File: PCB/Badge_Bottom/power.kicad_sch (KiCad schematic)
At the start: 10 parts, among them J2 BAT, SW3 MSK12C02-HB, U1 TP4054, U3 AMS1117-3.3

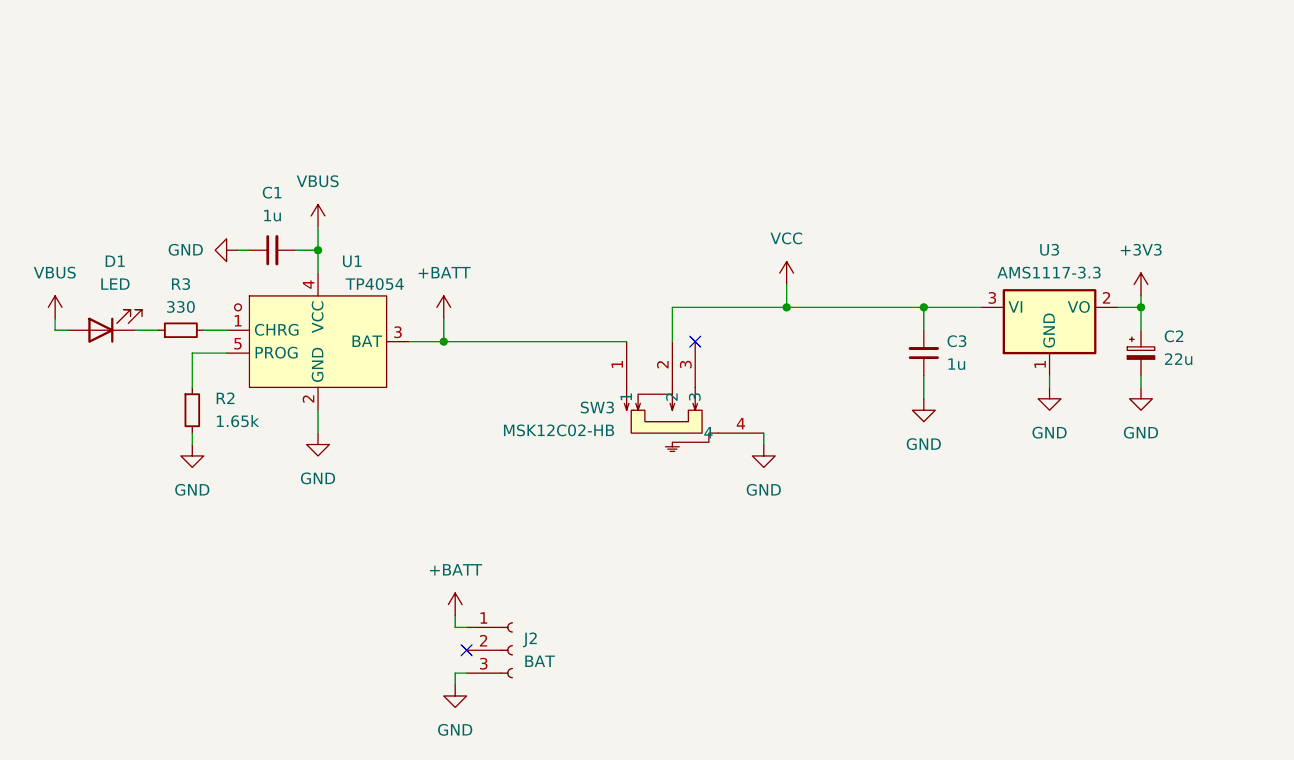
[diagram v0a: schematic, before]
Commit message: Added new page for IO, added new components, added JLC parts, fixed PCB standoffs to be pads and modified concept of PCB (dual usbc)
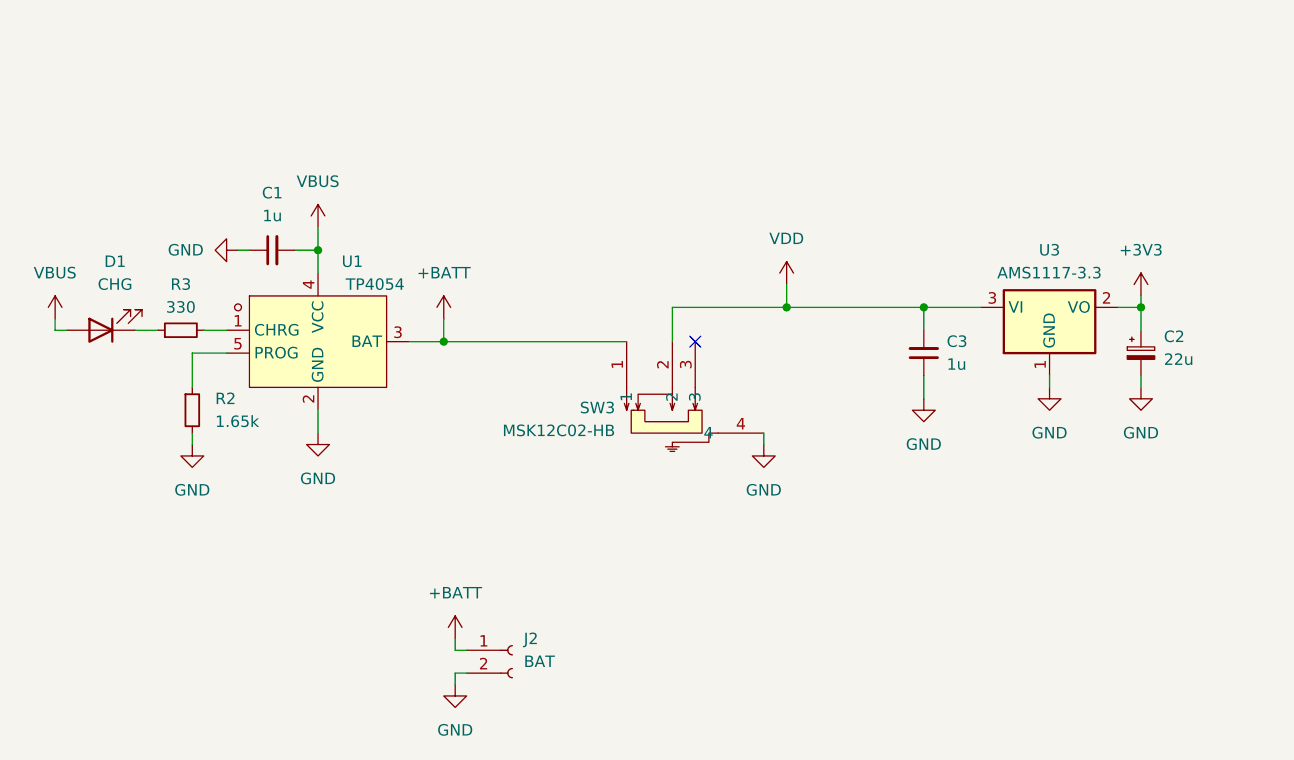
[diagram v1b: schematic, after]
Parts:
- C1, C2, C3: footprint (none) -> Capacitor_SMD:C_0603_1608Metric
- D1: value LED -> CHG; footprint (none) -> LED_SMD:LED_0603_1608Metric
- J2: footprint (none) -> Connector_JST:JST_PH_S2B-PH-SM4-TB_1x02-1MP_P2.00mm_Horizontal; symbol Connector:Conn_01x03_Socket -> Connector:Conn_01x02_Socket
- R2, R3: footprint (none) -> Resistor_SMD:R_0603_1608Metric
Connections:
- net GND: now also J2.2 (Pin_2); no longer J2.3 (Pin_3)
- net VCC renamed VDD
- no-connect marks 2 -> 1
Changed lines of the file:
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@@
   )
   (no_connect (at 148.59 100.33))
-  (no_connect (at 123.19 134.62))
-  (wire (pts (xy 123.19 132.08) (xy 121.92 132.08))
-    (stroke (width 0) (type default))
-  )
   (wire (pts (xy 146.05 96.52) (xy 158.75 96.52))
     (stroke (width 0) (type default))
@@
     (stroke (width 0) (type default))
   )
-  (wire (pts (xy 121.92 130.81) (xy 121.92 132.08))
-    (stroke (width 0) (type default))
-  )
   (wire (pts (xy 120.65 100.33) (xy 120.65 97.79))
     (stroke (width 0) (type default))
@@
     (stroke (width 0) (type default))
   )
+  (wire (pts (xy 123.19 134.62) (xy 121.92 134.62))
+    (stroke (width 0) (type default))
+  )
   (wire (pts (xy 198.12 96.52) (xy 198.12 99.06))
     (stroke (width 0) (type default))
@@
     (stroke (width 0) (type default))
   )
+  (wire (pts (xy 121.92 134.62) (xy 121.92 133.35))
+    (stroke (width 0) (type default))
+  )
   (wire (pts (xy 97.79 90.17) (xy 99.06 90.17))
     (stroke (width 0) (type default))
@@
     (stroke (width 0) (type default))
   )
-  (symbol (lib_id "power:+BATT") (at 121.92 130.81 0) (unit 1)
-    (in_bom yes) (on_board yes) (dnp no) (fields_autoplaced)
-    (property "Reference" "#PWR07" (at 121.92 134.62 0)
-      (effects (font (size 1.27 1.27)) hide)
-    )
-    (property "Value" "+BATT" (at 121.92 125.73 0)
-      (effects (font (size 1.27 1.27)))
-    )
-    (property "Footprint" "" (at 121.92 130.81 0)
-      (effects (font (size 1.27 1.27)) hide)
-    )
-    (property "Datasheet" "" (at 121.92 130.81 0)
+  (symbol (lib_id "power:+BATT") (at 121.92 133.35 0) (unit 1)
+    (in_bom yes) (on_board yes) (dnp no) (fields_autoplaced)
+    (property "Reference" "#PWR07" (at 121.92 137.16 0)
+      (effects (font (size 1.27 1.27)) hide)
+    )
+    (property "Value" "+BATT" (at 121.92 128.27 0)
+      (effects (font (size 1.27 1.27)))
+    )
+    (property "Footprint" "" (at 121.92 133.35 0)
+      (effects (font (size 1.27 1.27)) hide)
+    )
+    (property "Datasheet" "" (at 121.92 133.35 0)
       (effects (font (size 1.27 1.27)) hide)
     )
@@
       (effects (font (size 1.27 1.27)))
     )
-    (property "Footprint" "" (at 91.44 99.06 0)
+    (property "Footprint" "Resistor_SMD:R_0603_1608Metric" (at 91.44 99.06 0)
       (effects (font (size 1.27 1.27)) hide)
     )
@@
     )
   )
+  (symbol (lib_id "power:VDD") (at 158.75 93.98 0) (unit 1)
+    (in_bom yes) (on_board yes) (dnp no) (fields_autoplaced)
+    (property "Reference" "#PWR03" (at 158.75 97.79 0)
+      (effects (font (size 1.27 1.27)) hide)
+    )
+    (property "Value" "VDD" (at 158.75 88.9 0)
+      (effects (font (size 1.27 1.27)))
+    )
+    (property "Footprint" "" (at 158.75 93.98 0)
+      (effects (font (size 1.27 1.27)) hide)
+    )
+    (property "Datasheet" "" (at 158.75 93.98 0)
+      (effects (font (size 1.27 1.27)) hide)
+    )
+    (pin "1")
+    (instances
+      (project "Badge_Top"
+        (path "/9b902332-c8c9-42a9-accd-28597791eb2a"
+          (reference "#PWR03") (unit 1)
+        )
+      )
+      (project "Badge_Bottom"
+        (path "/9bea0129-61af-4534-9a88-a88b63234707"
+          (reference "#PWR021") (unit 1)
+        )
+        (path "/9bea0129-61af-4534-9a88-a88b63234707/0f55777b-99bc-476f-91c2-8f0549bc7bba"
+          (reference "#PWR014") (unit 1)
+        )
+      )
+    )
+  )
   (symbol (lib_id "power:GND") (at 173.99 106.68 0) (unit 1)
     (in_bom yes) (on_board yes) (dnp no) (fields_autoplaced)
@@
     )
   )
-  (symbol (lib_id "Connector:Conn_01x03_Socket") (at 128.27 134.62 0) (unit 1)
+  (symbol (lib_id "Connector:Conn_01x02_Socket") (at 128.27 134.62 0) (unit 1)
     (in_bom yes) (on_board yes) (dnp no) (fields_autoplaced)
     (property "Reference" "J2" (at 129.54 133.35 0)
@@
       (effects (font (size 1.27 1.27)) (justify left))
     )
-    (property "Footprint" "" (at 128.27 134.62 0)
+    (property "Footprint" "Connector_JST:JST_PH_S2B-PH-SM4-TB_1x02-1MP_P2.00mm_Horizontal" (at 128.27 134.62 0)
       (effects (font (size 1.27 1.27)) hide)
     )
@@
     (pin "1")
     (pin "2")
-    (pin "3")
     (instances
       (project "Badge_Bottom"
@@
         )
         (path "/9bea0129-61af-4534-9a88-a88b63234707/0f55777b-99bc-476f-91c2-8f0549bc7bba"
-          (reference "J2") (unit 1)
+          (reference "J3") (unit 1)
         )
       )
@@
       (effects (font (size 1.27 1.27)) (justify left))
     )
-    (property "Footprint" "" (at 198.12 101.6 0)
+    (property "Footprint" "Capacitor_SMD:C_0603_1608Metric" (at 198.12 101.6 0)
       (effects (font (size 1.27 1.27)) hide)
     )
@@
       (effects (font (size 1.27 1.27)))
     )
-    (property "Value" "LED" (at 84.1375 93.98 0)
-      (effects (font (size 1.27 1.27)))
-    )
-    (property "Footprint" "" (at 82.55 99.06 0)
+    (property "Value" "CHG" (at 84.1375 93.98 0)
+      (effects (font (size 1.27 1.27)))
+    )
+    (property "Footprint" "LED_SMD:LED_0603_1608Metric" (at 82.55 99.06 0)
       (effects (font (size 1.27 1.27)) hide)
     )
@@
     )
   )
-  (symbol (lib_id "power:VCC") (at 158.75 93.98 0) (unit 1)
-    (in_bom yes) (on_board yes) (dnp no) (fields_autoplaced)
-    (property "Reference" "#PWR014" (at 158.75 97.79 0)
-      (effects (font (size 1.27 1.27)) hide)
-    )
-    (property "Value" "VCC" (at 158.75 88.9 0)
-      (effects (font (size 1.27 1.27)))
-    )
-    (property "Footprint" "" (at 158.75 93.98 0)
-      (effects (font (size 1.27 1.27)) hide)
-    )
-    (property "Datasheet" "" (at 158.75 93.98 0)
-      (effects (font (size 1.27 1.27)) hide)
-    )
-    (pin "1")
-    (instances
-      (project "Badge_Bottom"
-        (path "/9bea0129-61af-4534-9a88-a88b63234707/0f55777b-99bc-476f-91c2-8f0549bc7bba"
-          (reference "#PWR014") (unit 1)
-        )
-      )
-    )
-  )
   (symbol (lib_id "Device:C_Small") (at 173.99 101.6 180) (unit 1)
     (in_bom yes) (on_board yes) (dnp no) (fields_autoplaced)
@@
       (effects (font (size 1.27 1.27)) (justify right))
     )
-    (property "Footprint" "" (at 173.99 101.6 0)
+    (property "Footprint" "Capacitor_SMD:C_0603_1608Metric" (at 173.99 101.6 0)
       (effects (font (size 1.27 1.27)) hide)
     )
@@
       (effects (font (size 1.27 1.27)) (justify left))
     )
-    (property "Footprint" "" (at 92.71 107.95 0)
+    (property "Footprint" "Resistor_SMD:R_0603_1608Metric" (at 92.71 107.95 0)
       (effects (font (size 1.27 1.27)) hide)
     )
@@
       (effects (font (size 1.27 1.27)))
     )
-    (property "Footprint" "" (at 101.6 90.17 0)
-      (effects (font (size 1.27 1.27)) hide)
-    )
+    (property "Footprint" "Capacitor_SMD:C_0603_1608Metric" (at 101.6 90.17 0)
+      (effects (font (size 1.27 1.27)) hide)
+    )

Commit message: finished schematic and added jlc parts
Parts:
- removed C2: 22u, Capacitor_SMD:C_0603_1608Metric, symbol Device:C_Polarized_Small
- removed U3: AMS1117-3.3, Package_TO_SOT_SMD:SOT-223-3_TabPin2, symbol Regulator_Linear:AMS1117-3.3
- added C2: 1u, Capacitor_SMD:C_0603_1608Metric, symbol Device:C_Small
- added U4: XC6206PxxxMR, Package_TO_SOT_SMD:SOT-23-3, symbol Regulator_Linear:XC6206PxxxMR
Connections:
- net +3V3: now also C2.2, U4.2 (VO)
- net GND: now also C2.1, U4.1 (GND)
- net VDD: now also U4.3 (VI)
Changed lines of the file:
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@@
+    )
+  )
+  (symbol (lib_id "Regulator_Linear:XC6206PxxxMR") (at 187.96 96.52 0) (unit 1)
+    (in_bom yes) (on_board yes) (dnp no) (fields_autoplaced)
+    (property "Reference" "U4" (at 187.96 90.17 0)
+      (effects (font (size 1.27 1.27)))
+    )
+    (property "Value" "XC6206PxxxMR" (at 187.96 92.71 0)
+      (effects (font (size 1.27 1.27)))
+    )
+    (property "Footprint" "Package_TO_SOT_SMD:SOT-23-3" (at 187.96 90.805 0)
+      (effects (font (size 1.27 1.27) italic) hide)
+    )
+    (property "Datasheet" "https://www.torexsemi.com/file/xc6206/XC6206.pdf" (at 187.96 96.52 0)
+      (effects (font (size 1.27 1.27)) hide)
+    )
+    (pin "1")
+    (pin "2")
+    (pin "3")
+    (instances
+      (project "Badge_Bottom"
+        (path "/9bea0129-61af-4534-9a88-a88b63234707/0f55777b-99bc-476f-91c2-8f0549bc7bba"
+          (reference "U4") (unit 1)
+        )
+      )
     )
   )
@@
     )
   )
-  (symbol (lib_id "Device:C_Polarized_Small") (at 198.12 101.6 0) (unit 1)
-    (in_bom yes) (on_board yes) (dnp no) (fields_autoplaced)
-    (property "Reference" "C2" (at 200.66 99.7839 0)
-      (effects (font (size 1.27 1.27)) (justify left))
-    )
-    (property "Value" "22u" (at 200.66 102.3239 0)
-      (effects (font (size 1.27 1.27)) (justify left))
-    )
-    (property "Footprint" "Capacitor_SMD:C_0603_1608Metric" (at 198.12 101.6 0)
-      (effects (font (size 1.27 1.27)) hide)
-    )
-    (property "Datasheet" "~" (at 198.12 101.6 0)
-      (effects (font (size 1.27 1.27)) hide)
-    )
-    (pin "1")
-    (pin "2")
-    (instances
-      (project "Badge_Bottom"
-        (path "/9bea0129-61af-4534-9a88-a88b63234707/0f55777b-99bc-476f-91c2-8f0549bc7bba"
-          (reference "C2") (unit 1)
-        )
-      )
-    )
-  )
   (symbol (lib_id "Device:LED") (at 82.55 99.06 180) (unit 1)
     (in_bom yes) (on_board yes) (dnp no) (fields_autoplaced)
@@
         (path "/9bea0129-61af-4534-9a88-a88b63234707/0f55777b-99bc-476f-91c2-8f0549bc7bba"
           (reference "D1") (unit 1)
-        )
-      )
-    )
-  )
-  (symbol (lib_id "Regulator_Linear:AMS1117-3.3") (at 187.96 96.52 0) (unit 1)
-    (in_bom yes) (on_board yes) (dnp no) (fields_autoplaced)
-    (property "Reference" "U3" (at 187.96 90.17 0)
-      (effects (font (size 1.27 1.27)))
-    )
-    (property "Value" "AMS1117-3.3" (at 187.96 92.71 0)
-      (effects (font (size 1.27 1.27)))
-    )
-    (property "Footprint" "Package_TO_SOT_SMD:SOT-223-3_TabPin2" (at 187.96 91.44 0)
-      (effects (font (size 1.27 1.27)) hide)
-    )
-    (property "Datasheet" "http://www.advanced-monolithic.com/pdf/ds1117.pdf" (at 190.5 102.87 0)
-      (effects (font (size 1.27 1.27)) hide)
-    )
-    (pin "1")
-    (pin "2")
-    (pin "3")
-    (instances
-      (project "Badge_Bottom"
-        (path "/9bea0129-61af-4534-9a88-a88b63234707/0f55777b-99bc-476f-91c2-8f0549bc7bba"
-          (reference "U3") (unit 1)
         )
       )
@@
         )
       )
+    )
+  )
+  (symbol (lib_id "Device:C_Small") (at 198.12 101.6 180) (unit 1)
+    (in_bom yes) (on_board yes) (dnp no) (fields_autoplaced)
+    (property "Reference" "C2" (at 200.66 100.3236 0)
+      (effects (font (size 1.27 1.27)) (justify right))
+    )
+    (property "Value" "1u" (at 200.66 102.8636 0)
+      (effects (font (size 1.27 1.27)) (justify right))
+    )
+    (property "Footprint" "Capacitor_SMD:C_0603_1608Metric" (at 198.12 101.6 0)
+      (effects (font (size 1.27 1.27)) hide)
+    )
+    (property "Datasheet" "~" (at 198.12 101.6 0)
+      (effects (font (size 1.27 1.27)) hide)
+    )
+    (pin "1")
+    (pin "2")
+    (instances
+      (project "Badge_Bottom"
+        (path "/9bea0129-61af-4534-9a88-a88b63234707/0f55777b-99bc-476f-91c2-8f0549bc7bba"
+          (reference "C2") (unit 1)
+        )
+      )

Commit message: finised pcb layout
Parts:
- added TP1 (x5): TestPoint, TestPoint:TestPoint_Pad_D1.0mm, symbol Connector:TestPoint
- J2: footprint Connector_JST:JST_PH_S2B-PH-SM4-TB_1x02-1MP_P2.00mm_Horizontal -> JSTPH_Clone:CONN-SMD_2P-P2.00_XUNPU_WAFER-PH2.0-2PWB
- renumbered D1 to CHG1
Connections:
- net +3V3: now also TP1.1
- net +BATT: now also TP1.1
- net GND: now also J2.4 (MP), J2.5 (MP), TP1.1
- net VBUS: now also TP1.1
- net VDD: now also TP1.1
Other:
- note added: "Battery Connector JST PH 2Pin SMD Horizontal"
- note added: "TP4054 Charging Controller"
- note added: "XC6206 LDO 3.3V"
- moved on the sheet: C1, C2, C3, CHG1, R2, R3, SW3, U1, U4

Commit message: Added docs and readme, ordered PCBs at JLC
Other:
- company: (none) -> Unterland
- title: (none) -> Unterland Badge Bottom
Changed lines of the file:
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@@
 (kicad_sch (version 20230121) (generator eeschema)
   (paper "A4")
+  (title_block
+    (title "Unterland Badge Bottom")
+    (date "2023-07-29")
+    (rev "1")
+    (company "Unterland")
+    (comment 1 "Power Section")
+  )
   (junction (at 172.72 85.09) (diameter 0) (color 0 0 0 0)
   )
